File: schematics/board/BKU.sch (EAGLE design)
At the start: 68 parts, among them Q1 8MHz, Q2 32,768KHz, U1 STM32F405RGT6

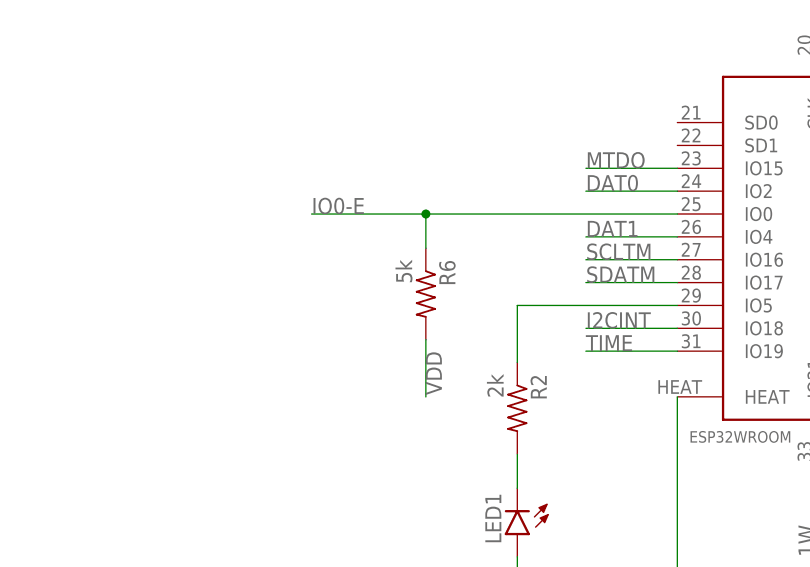
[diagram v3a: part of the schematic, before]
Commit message: Добавлены светодиоды на платы БСК
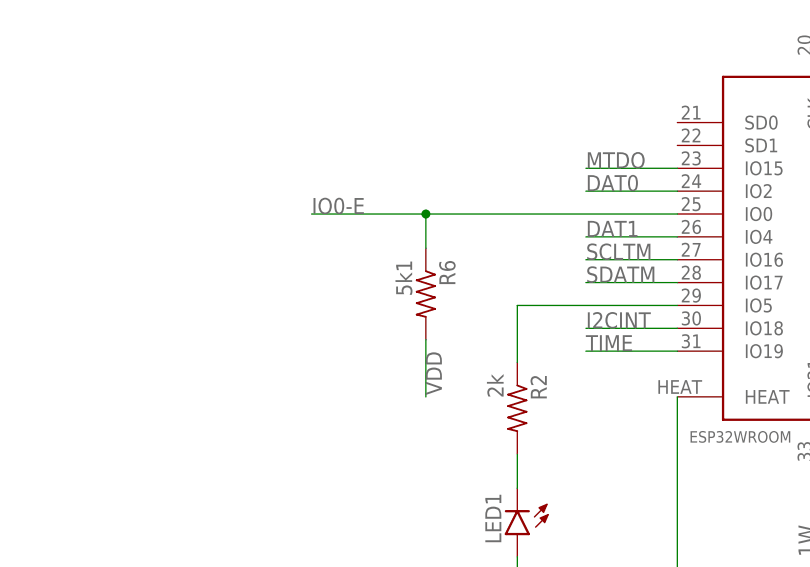
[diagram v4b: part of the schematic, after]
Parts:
- R6: value 5k -> 5k1
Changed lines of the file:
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@@
 <part name="C4" library="rcl" library_urn="urn:adsk.eagle:library:334" deviceset="C-US" device="C0603" package3d_urn="urn:adsk.eagle:package:23616/2" value="1nF"/>
 <part name="R5" library="resistor" library_urn="urn:adsk.eagle:library:348" deviceset="R-US_" device="R0603" package3d_urn="urn:adsk.eagle:package:23555/3" value="12k"/>
-<part name="R6" library="resistor" library_urn="urn:adsk.eagle:library:348" deviceset="R-US_" device="R0603" package3d_urn="urn:adsk.eagle:package:23555/3" value="5k"/>
+<part name="R6" library="resistor" library_urn="urn:adsk.eagle:library:348" deviceset="R-US_" device="R0603" package3d_urn="urn:adsk.eagle:package:23555/3" value="5k1"/>
 <part name="U$4" library="CanCubeSat" deviceset="USB-C" device=""/>
 <part name="U$6" library="CanCubeSat" deviceset="USB-C" device=""/>

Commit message: Добавлена плата MAG
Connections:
- new net RX-ES: U$13.IO22, U1.PB9
- new net TX-ES: U$13.IO23, U1.PB10
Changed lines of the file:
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@@
 <?xml version="1.0" encoding="utf-8"?>
 <!DOCTYPE eagle SYSTEM "eagle.dtd">
-<eagle version="9.5.1">
+<eagle version="9.6.0">
 <drawing>
 <settings>
@@
 </segment>
 </net>
+<net name="RX-ES" class="0">
+<segment>
+<pinref part="U$13" gate="G$1" pin="IO22"/>
+<wire x1="66.04" y1="27.94" x2="66.04" y2="17.78" width="0.1524" layer="91"/>
+<label x="66.04" y="17.78" size="1.778" layer="95" rot="R90"/>
+</segment>
+<segment>
+<pinref part="U1" gate="G$1" pin="PB9"/>
+<wire x1="231.14" y1="93.98" x2="215.9" y2="93.98" width="0.1524" layer="91"/>
+<label x="215.9" y="93.98" size="1.778" layer="95"/>
+</segment>
+</net>
+<net name="TX-ES" class="0">
+<segment>
+<pinref part="U$13" gate="G$1" pin="IO23"/>
+<wire x1="68.58" y1="27.94" x2="68.58" y2="17.78" width="0.1524" layer="91"/>
+<label x="68.58" y="17.78" size="1.778" layer="95" rot="R90"/>
+</segment>
+<segment>
+<pinref part="U1" gate="G$1" pin="PB10"/>
+<wire x1="231.14" y1="91.44" x2="215.9" y2="91.44" width="0.1524" layer="91"/>
+<label x="215.9" y="91.44" size="1.778" layer="95"/>
+</segment>
+</net>

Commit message: Исправлены компоненты
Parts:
- removed R28, R29, R30, R31, R32: 3.3, resistor-shunt:SMK
- added MAG: (no value), pinheadCS:PINHD-1X4
- added R15: 2k, resistor:R-US_R0603
- added R21, R22, R23, R24: 3k3, resistor:R-US_R0603
- added R25, R26: 5k1, resistor:R-US_R0603
- Q2: device 9C-8.000MEEJ-T:9C-8.000MEEJ-T -> CanCubeSat:C005R
- R1, R14, R3, R4: device resistor-shunt:BVS -> resistor:R-US_R0603
- R16: value 1M -> 2k; device resistor-shunt:BVS -> resistor:R-US_R0603
- R17: value 2k -> 1M; device resistor-shunt:BVS -> resistor:R-US_R0603
- R18: value 2k -> 3k3; device resistor-shunt:BVS -> resistor:R-US_R0603
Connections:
- new net SCL: MAG.3, R25.2, U1.PB10
- new net SDA: MAG.4, R26.2, U1.PB11
- new net TIME-ES: U$13.SVN
- new net TIME-G: U$1.PPS
- net DAT0: now also R23.2; no longer R29.1
- net DAT1: now also R24.2; no longer R30.1
- net GND: now also MAG.1, R16.1; no longer R18.1
- net MTCK: now also R21.2; no longer R31.1
- net MTDI: now also R18.2; no longer R32.1
- net MTDO: now also R22.2; no longer R28.1
- net N$11: now also R14.1; no longer R14.2
- net N$12: now also R4.1; no longer R4.2
- net N$15: now also R17.1; no longer R16.2
- net N$30: now also R17.2; no longer R16.1
- net N$37: now also R15.2; no longer R17.1
- net N$38: now also R15.1; no longer R17.2
- net N$40: now also R16.2; no longer R18.2
- net RX-ES: now also U1.PA9; no longer U1.PB9
- net RX-S: now also U1.PC10
- net SWC: now also R3.1; no longer R3.2
- net SWD: now also R1.1; no longer R1.2
- net TX-ES: now also U1.PA10; no longer U1.PB10
- net TX-S: now also U1.PC11
- net VDD: now also MAG.2, R1.2, R14.2, R18.1, R21.1, R22.1, R23.1, R24.1, R25.1, R26.1, R3.2, R4.2; no longer R1.1, R14.1, R28.2, R29.2, R3.1, R30.2, R31.2, R32.2, R4.1
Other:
- moved on the sheet: C2, D3, D4

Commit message: Незначительные изменения БКУ
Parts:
- removed C13, C9: 47µ, rcl:C-USC1206
- removed D3, D4: HLMP6, display-hp:HLMP6
- removed U$3: CD, untitled:CD
- added C12: 0,1µ, rcl:C-USC0603
- added C17: 47µ, rcl:C-USC1206
- added LED-B#2, LED-G#2, LED2, LED3: (no value), led:LEDCHIPLED_0603
- added R27, R28: 2k, resistor:R-US_R0603
- added U$14: SD, CanCubeSat:SD
- C16: value 0.1u -> 47µ; device rcl:C-EU025-024X044 -> rcl:C-USC1206
- U$1: value NEO -> GPS; device untitled:NEO -> CanCubeSat:GPS
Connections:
- removed net N$36: C13.1, C9.2
- new net GND2: R27.2
- new net N$50: LED-B#2.A
- new net N$51: LED-B#2.C, R27.1
- new net N$52: LED-G#2.C, R28.2
- net 5V: now also R28.1
- net B2_KEM+: now also U$19.Q6; no longer U$18.Q6
- net B2_KEM-: now also U$19.Q7; no longer U$18.Q7
- net B2_KHEAT: now also U$19.Q5; no longer U$18.Q5
- net B2_KVCC: now also U$19.Q4; no longer U$18.Q4
- net B4_KEM+: now also U$18.Q6; no longer U$19.Q6
- net B4_KEM-: now also U$18.Q7; no longer U$19.Q7
- net B4_KHEAT: now also U$18.Q5; no longer U$19.Q5
- net B4_KVCC: now also U$18.Q4; no longer U$19.Q4
- net BUS+: now also C16.1, C17.1; no longer C9.1
- net BUS-: now also LED-G#2.A
- net DAT0: now also U$14.DAT0; no longer U$3.DAT0
- net DAT1: now also U$14.DAT1; no longer U$3.DAT1
- net GND: now also C12.1, C16.2, C17.2, U$14.VDD; no longer C13.2, C16.1, U$3.VDD
- net MTCK: now also U$14.DAT3; no longer U$3.CD/DAT3
- net MTDI: now also U$14.DAT2; no longer U$3.DAT2
- net MTDO: now also U$14.CMD; no longer U$3.CMD
- net MTMS: now also U$14.CLK; no longer U$3.CLK
- net N$37: now also LED2.C; no longer D3.K
- net N$40: now also LED3.C; no longer D4.K
- net VDD: now also C12.2, LED2.A, LED3.A, U$14.VSS; no longer C16.2, D3.A, D4.A, U$3.VSS
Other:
- moved on the sheet: C16

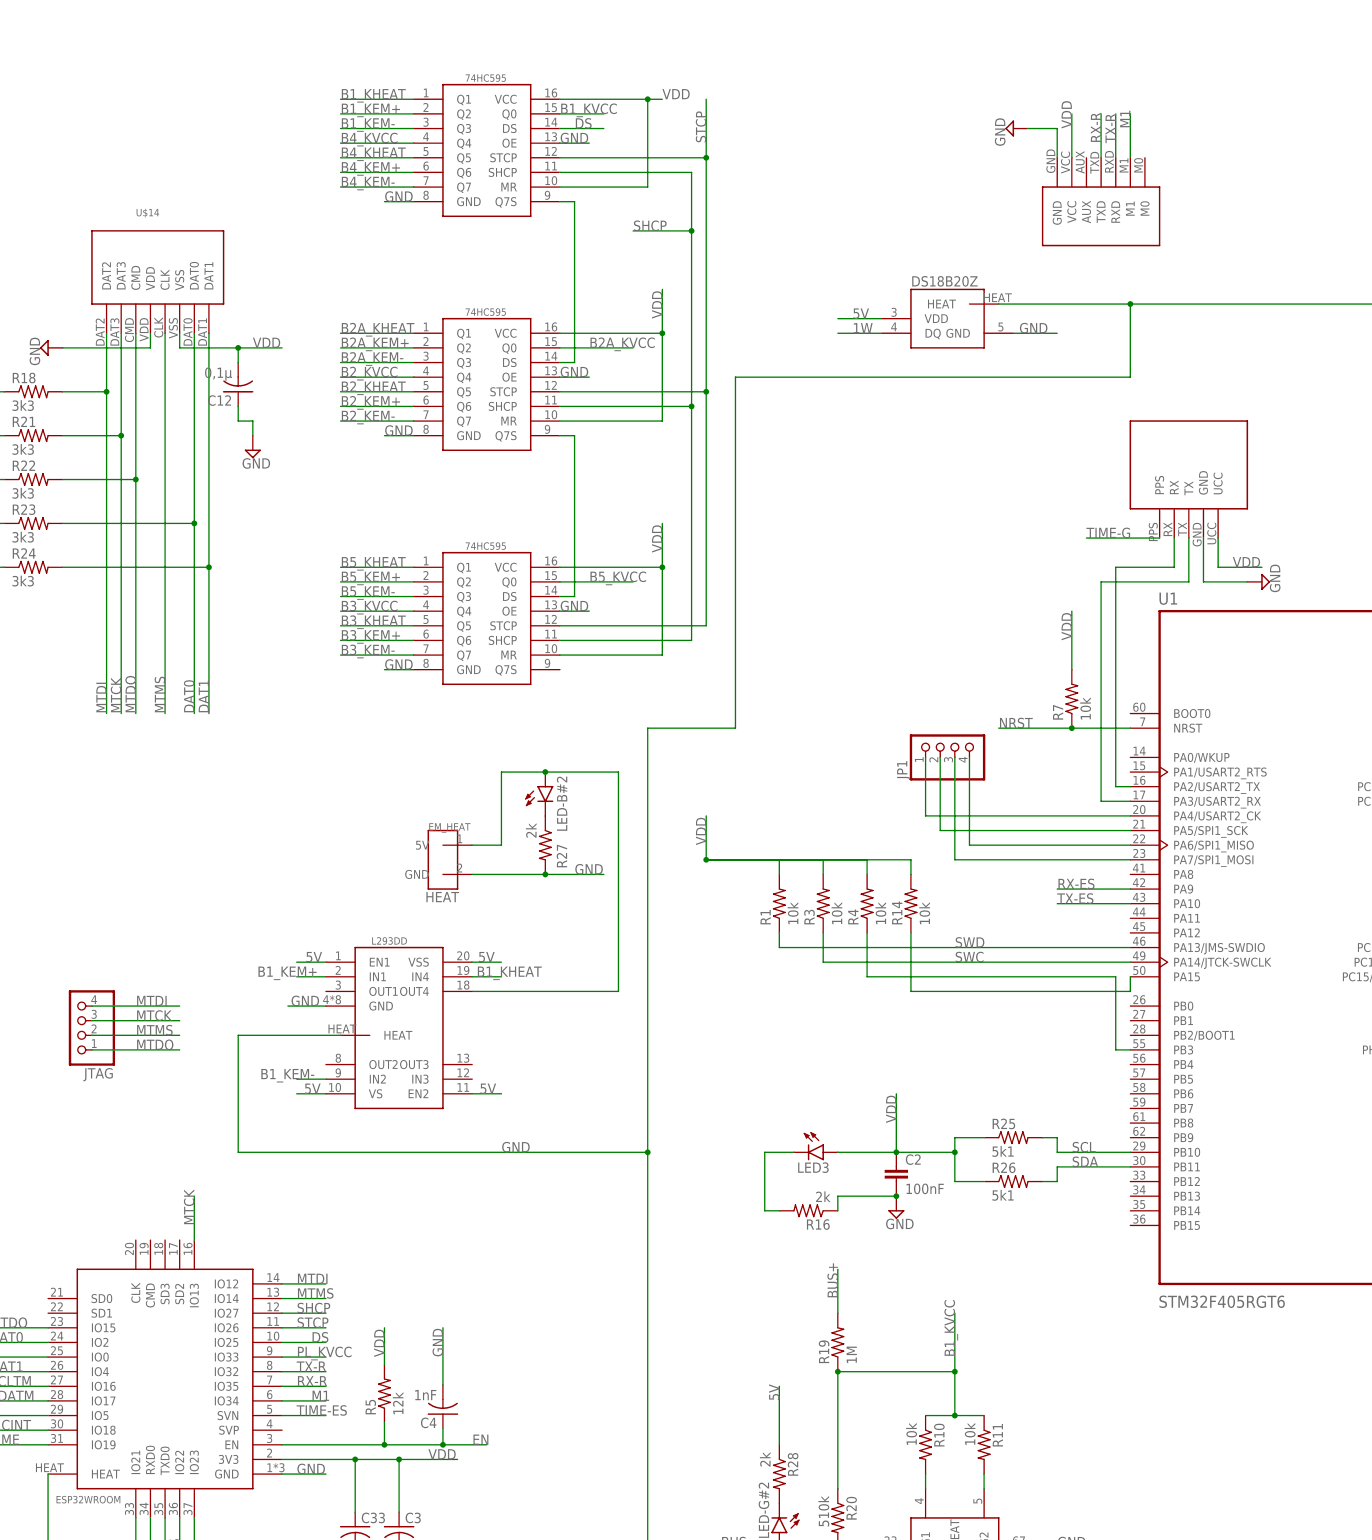
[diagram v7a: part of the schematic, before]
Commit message: Добавлена плата RADIO
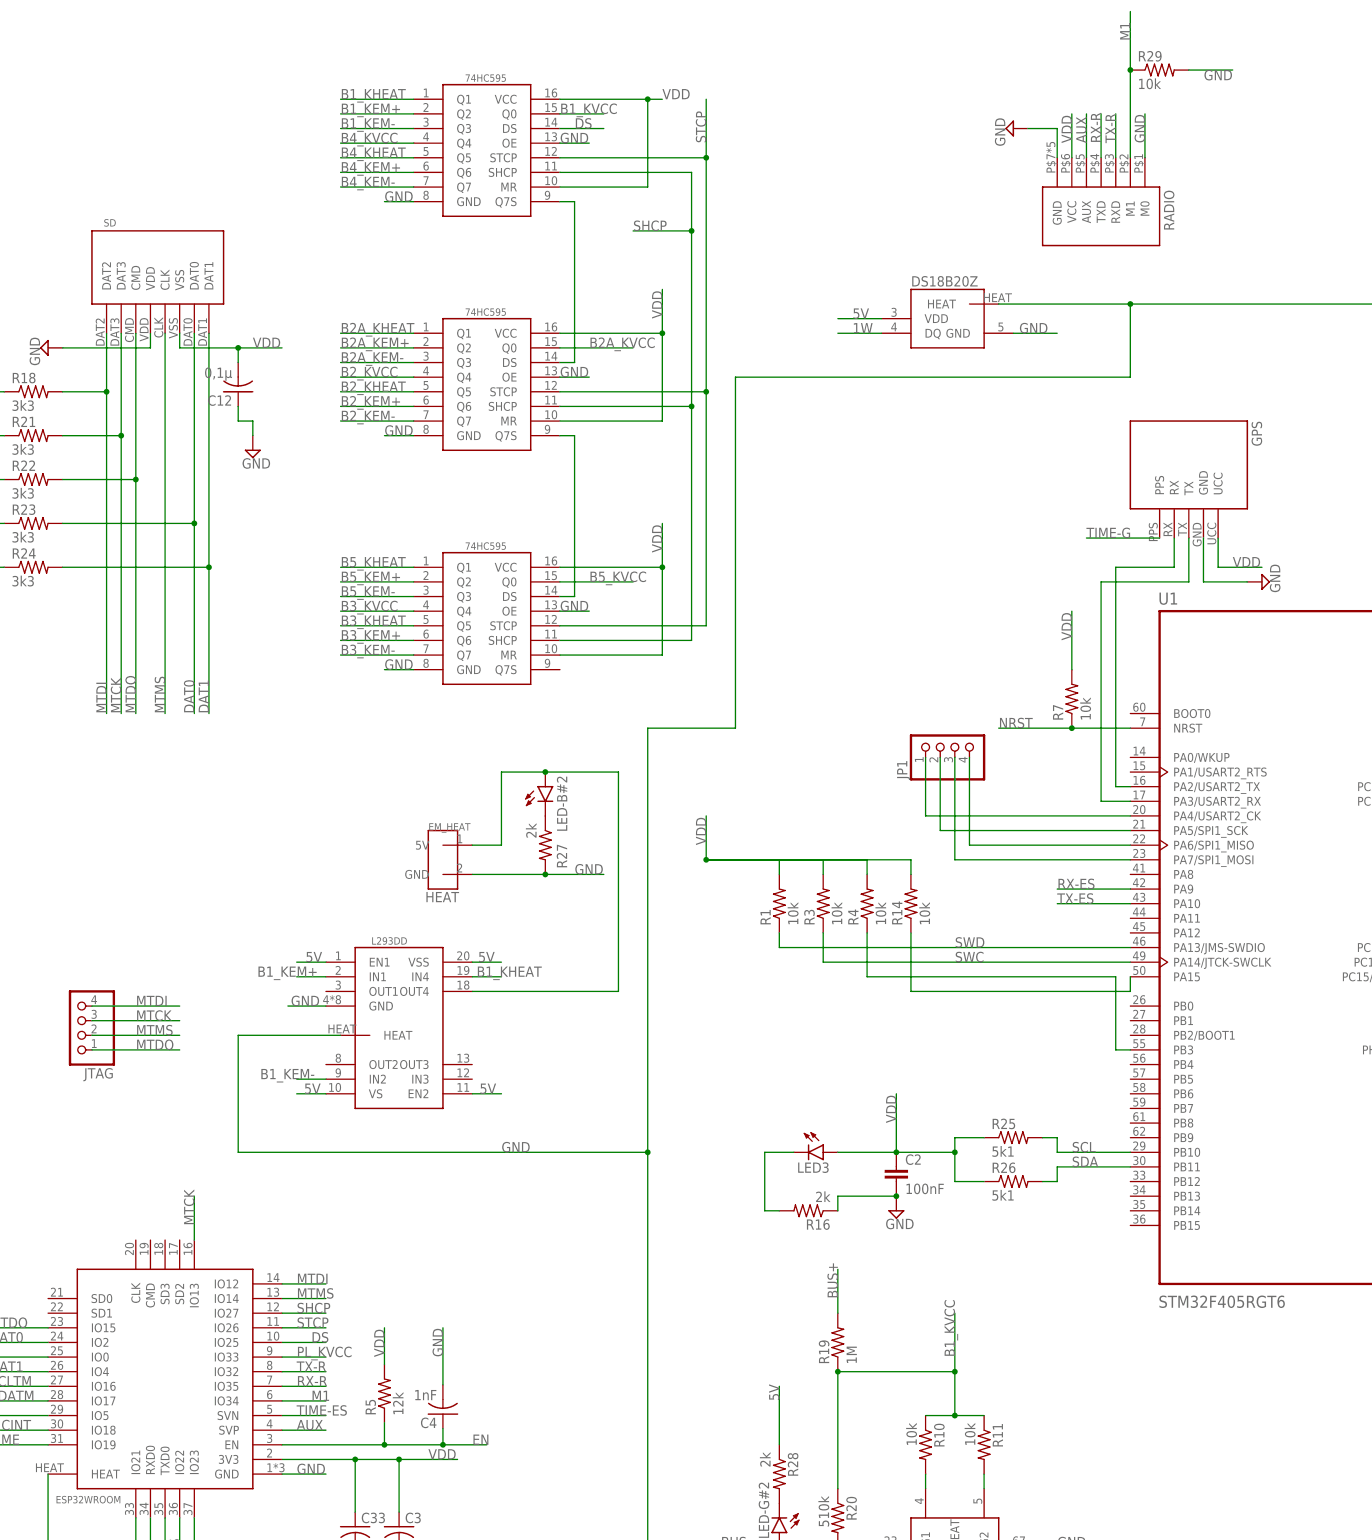
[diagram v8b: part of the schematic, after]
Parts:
- removed U$2: RADIO, untitled:RADIO
- added R29: 10k, resistor:R-US_R0603
- added RADIO: RADIO, CanCubeSat:RADIO
- renumbered U$1 to GPS, U$14 to SD
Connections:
- new net AUX: RADIO.AUX, U$13.SVP
- net GND: now also R29.2, RADIO.GND, RADIO.M0; no longer U$2.GND
- net M1: now also R29.1, RADIO.M1; no longer U$2.M1
- net RX-R: now also RADIO.TXD; no longer U$2.TXD
- net TX-R: now also RADIO.RXD; no longer U$2.RXD
- net VDD: now also RADIO.VCC; no longer U$2.VCC
